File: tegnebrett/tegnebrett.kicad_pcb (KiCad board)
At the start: 6 copper layers, 195.2 x 101 mm, 204 parts, among them J1 FH12-45S-0.5SH55, J2 FH12-6S-1SH55, J3 Conn_ST_STDC14, J4 USB-A1HSW6, J5 MCU_Header_Pin, J6 FPGA_debug, J7 FPGA_Header_Pin, J8 DA15_Socket, J9 PJ-002A, SW1 SW_Push, SW2 SW_Push, SW3 MCU_Button, SW4 Reset, SW5 Undo, SW6 FPGA_Button, U1 STM32U5G7VJTxQ, U2 XC7A100T-2FTG256I, U3 Oscillator 100MHz, U4 IS66WVH16M8DBLL-100B1LI1, U5 VGA Transceiver, U6 VGA Transciever, U7 TPS54294PWP2, U8 TPS54294PWP1, Y1 48MHz

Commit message: feat: latest PCB changes
We have 3 warnings and 3 errors, something like that. But should be
quick to fix.
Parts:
- C23, C24, C25, C26: moved to B.Cu
- FPGA Debug: renamed from J6
- FPGA GPIO: renamed from J7
- LCD Reset: renamed from SW1
- MCU Debug: renamed from J3
- MCU GPIO: renamed from J5
- moved C24 32.6 mm to (46.0, 83.0), turned to 180 degrees
- moved C26 32.3 mm to (46.0, 80.8), turned to 180 degrees
- moved C23 15.7 mm to (46.0, 58.0), turned to 180 degrees
- moved C25 15.0 mm to (46.0, 60.0), turned to 180 degrees
- renumbered JP1 to 1V0, JP4 to 1V8, JP2 to 3V3, JP3 to 5V, SW4 to Reset, SW3 to SW1, SW6 to SW3, F1 to U9, J4 to USB, SW5 to Undo
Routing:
- net +1V8: track 175.5 -> 382.6 mm, vias 4 -> 6
- net +1V0: track 201.1 -> 330.9 mm
- net +3V3: track 420.5 -> 340.5 mm, vias 53 -> 59
- net GND: track 614.1 -> 542.3 mm, vias 108 -> 125
- net Net-(U8-SW2): track 12.1 -> 17.8 mm
- net Net-(F1-SO1(IO1)): track 55.0 -> 57.8 mm
- net Net-(U7-EN2): track 17.2 -> 15.2 mm
- net /FPGA/VGA/R0: track 65.9 -> 67.2 mm
- net /MISO_FPGA: track 87.5 -> 88.7 mm
- net POWER_IN: track 171.4 -> 172.4 mm
- net /FPGA/VGA/R1: track 59.1 -> 59.7 mm
- net Net-(U8-VFB2): track 28.0 -> 28.6 mm
- net Net-(U7-VFB1): track 25.7 -> 26.2 mm
- added copper zone on In4.Cu, net +1V0
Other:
- board text added: "2025"

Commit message: feat: PCB updates
Latest changes from Tormod. Fixed warnings and errors.
Additionally moved the LCD screen connector ports to better fit the
actual LCD screen.
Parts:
- C69, C70, C71, C72, C75, C78: moved to B.Cu
- moved J2 3.17 mm to (86.2, 106.0)
- moved C69 2.53 mm to (203.9, 69.5)
- moved C72 1.61 mm to (186.1, 64.9), turned to 180 degrees
- moved C70 0.95 mm to (185.7, 68.7), turned to 180 degrees
- moved R5 0.90 mm to (89.8, 100.8)
- moved R1 0.67 mm to (83.3, 100.6)
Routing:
- net +1V8: track 382.6 -> 200.6 mm, vias 6 -> 5
- net +1V0: track 330.9 -> 198.0 mm, vias 6 -> 5
- net GND: track 542.3 -> 531.7 mm, vias 125 -> 147
- net POWER_IN: track 172.4 -> 178.3 mm, vias 2 -> 7
- net /TOUCH_WAKE: track 62.6 -> 58.1 mm
- net /TOUCH_SDA: track 82.2 -> 79.4 mm
- net +5V: track 97.7 -> 99.9 mm, vias 2 -> 1
- net /TOUCH_INT: track 58.6 -> 56.4 mm
- net /TOUCH_SCL: track 79.5 -> 77.4 mm
- net Net-(U8-EN2): track 29.1 -> 27.1 mm, vias 2 -> 3
- net Net-(U8-VREG5): track 5.63 -> 6.57 mm, vias 0 -> 2
- net Net-(U7-VREG5): track 6.73 -> 7.53 mm, vias 0 -> 2
- net /FPGA/VGA/B1: track 77.9 -> 77.2 mm
- net /FPGA/VGA/B0: track 78.1 -> 77.5 mm
- net /FPGA/VGA/B2: track 78.8 -> 78.2 mm

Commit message: fix: change layers to get correct impedance
GND is now on layer2, the USB-A stuff needs correct impedance.
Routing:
- added copper zone on In1.Cu, net GND
- removed copper zone on In3.Cu, net GND

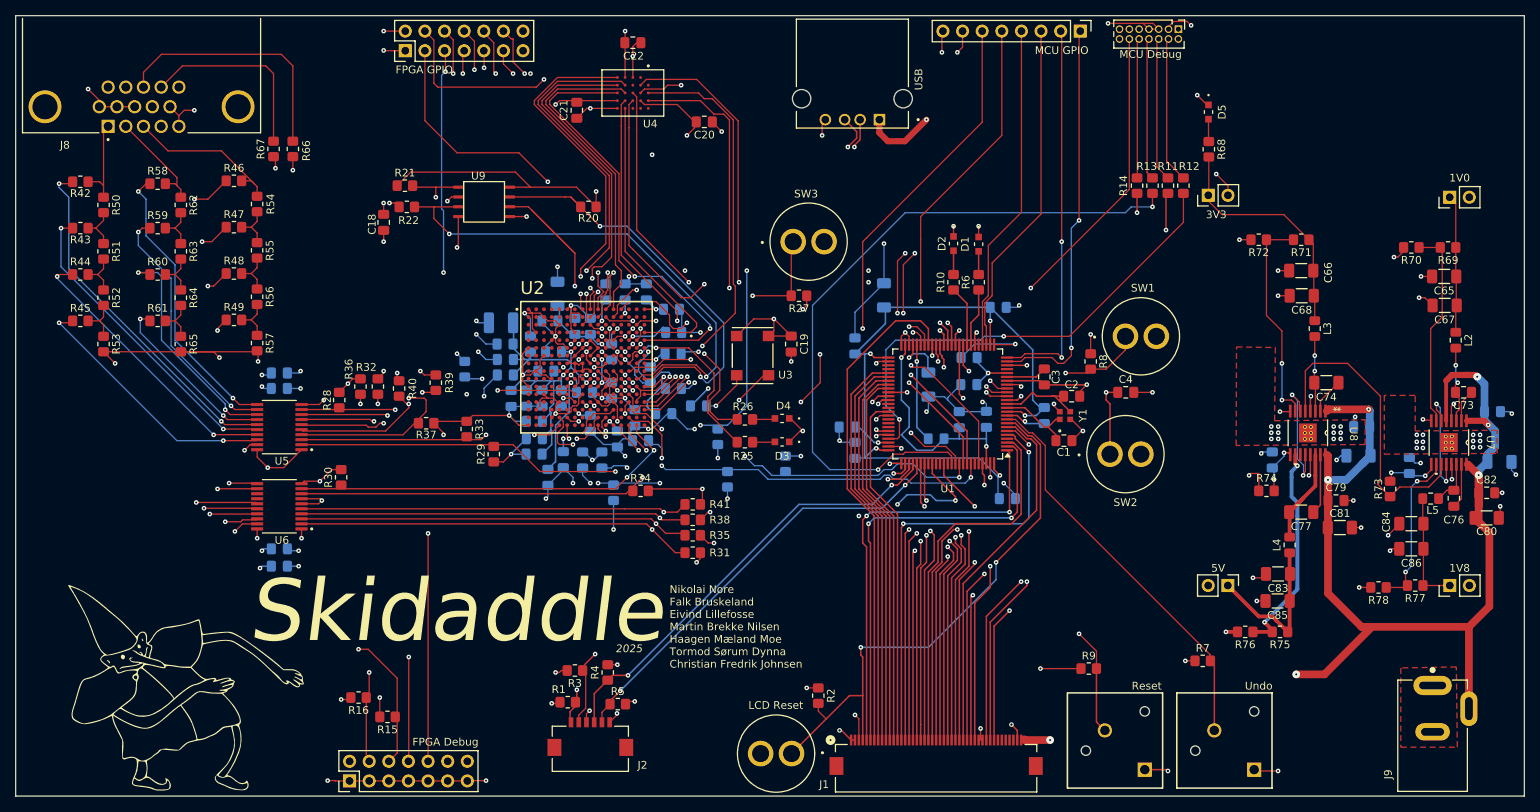
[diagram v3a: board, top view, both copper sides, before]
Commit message: fix: import LCD resistor to PCB
Again, this is to limit the current going through the LCD screen.
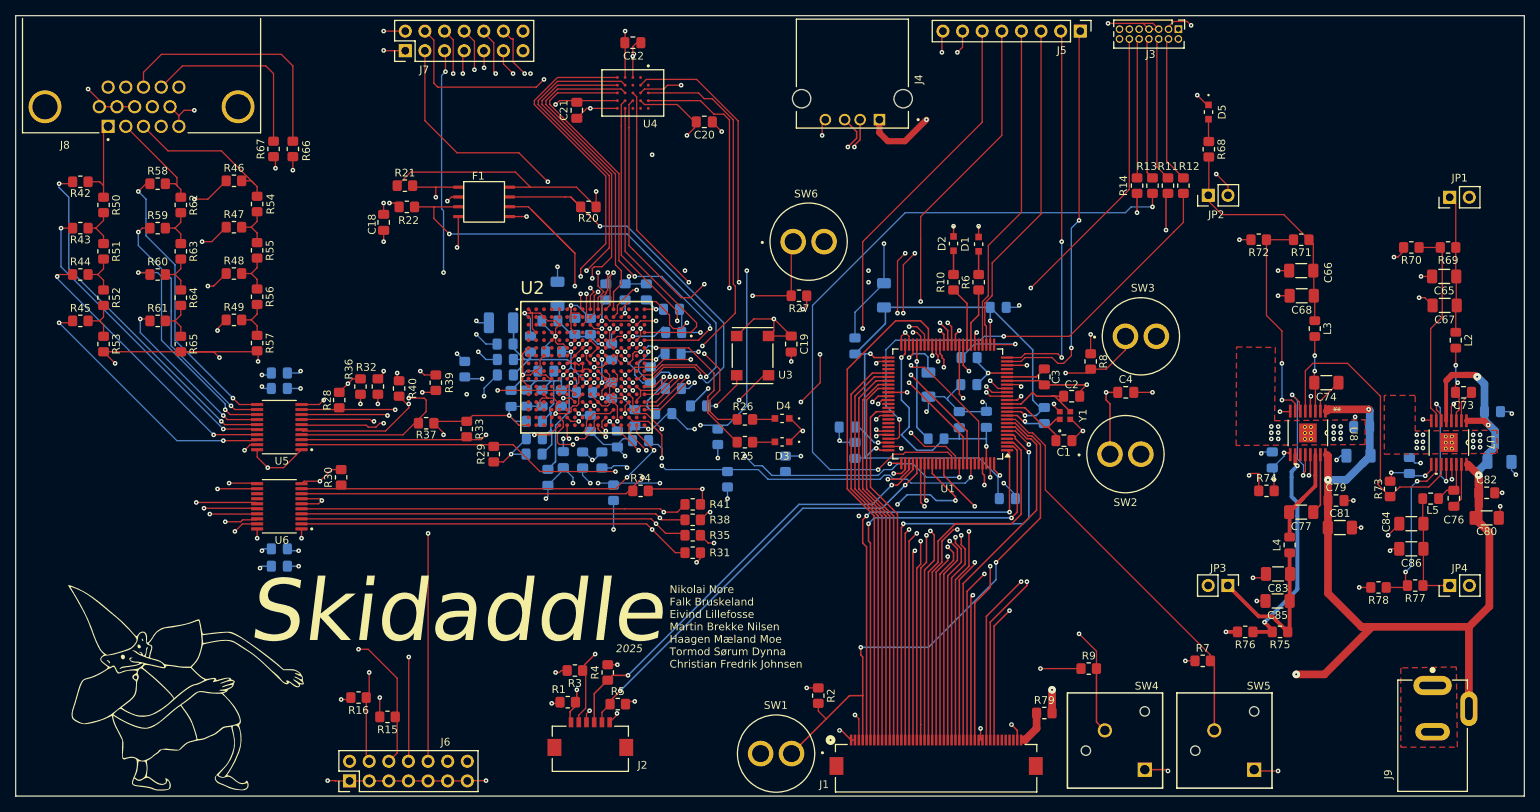
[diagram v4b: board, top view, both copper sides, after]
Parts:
- added R79: 12, Resistor_SMD:R_0805_2012Metric_Pad1.20x1.40mm_HandSolder, F.Cu at (145.0, 102.0)
- J3: renamed from MCU Debug
- J5: renamed from MCU GPIO
- J6: renamed from FPGA Debug
- J7: renamed from FPGA GPIO
- SW1: renamed from LCD Reset
- renumbered U9 to F1, USB to J4, 1V0 to JP1, 3V3 to JP2, 5V to JP3, 1V8 to JP4, SW1 to SW3, Reset to SW4, Undo to SW5, SW3 to SW6
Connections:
- J1 pad 45: POWER_IN -> Net-(J1-LED-A)
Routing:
- net Net-(J1-LED-A): track 0.00 -> 4.26 mm
- net POWER_IN: track 178.3 -> 175.2 mm
